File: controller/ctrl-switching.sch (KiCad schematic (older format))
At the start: 35 parts, among them U10 ULN2803A, U11 ULN2803A, U9 74HC595_WITH_PWR

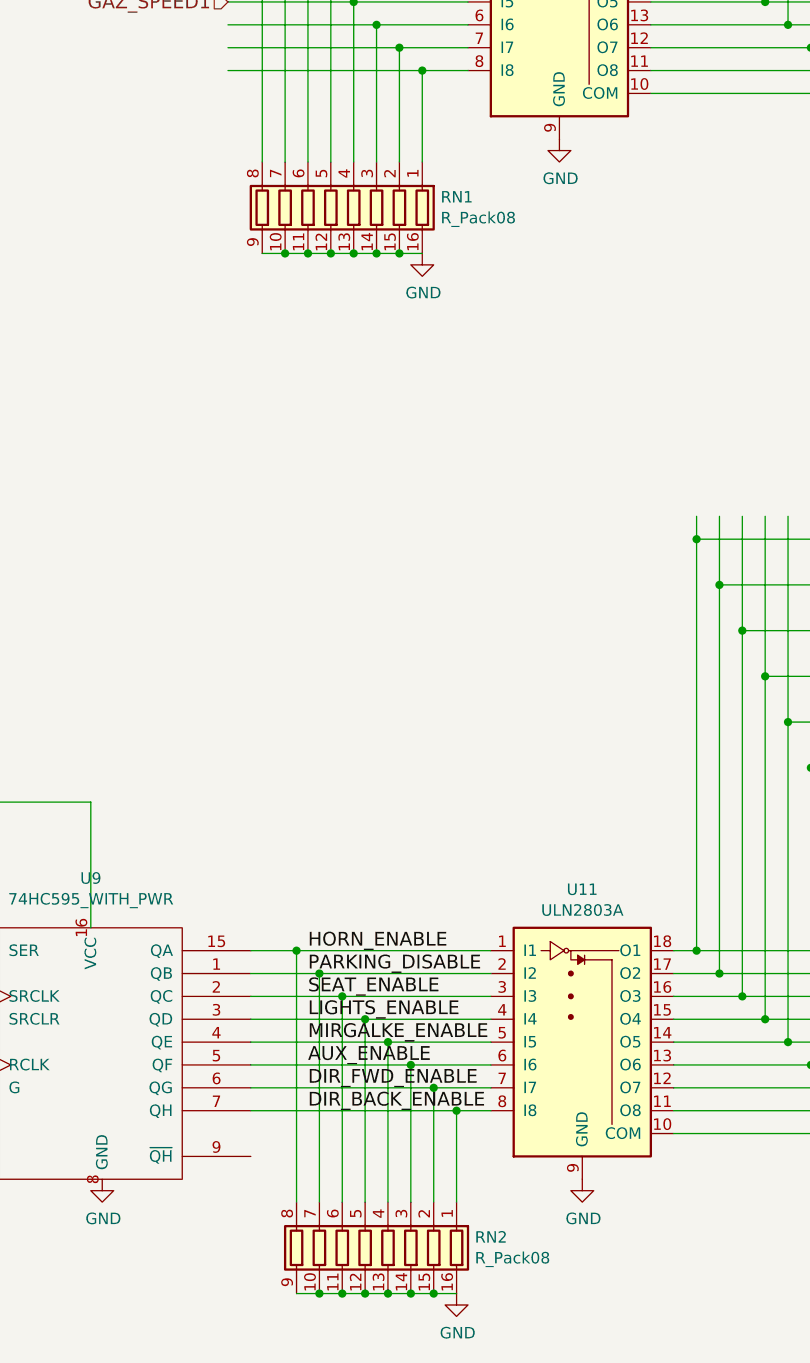
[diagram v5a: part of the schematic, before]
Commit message: Various fixes and comments to the controller board, also making it suitable for non-plated holes.
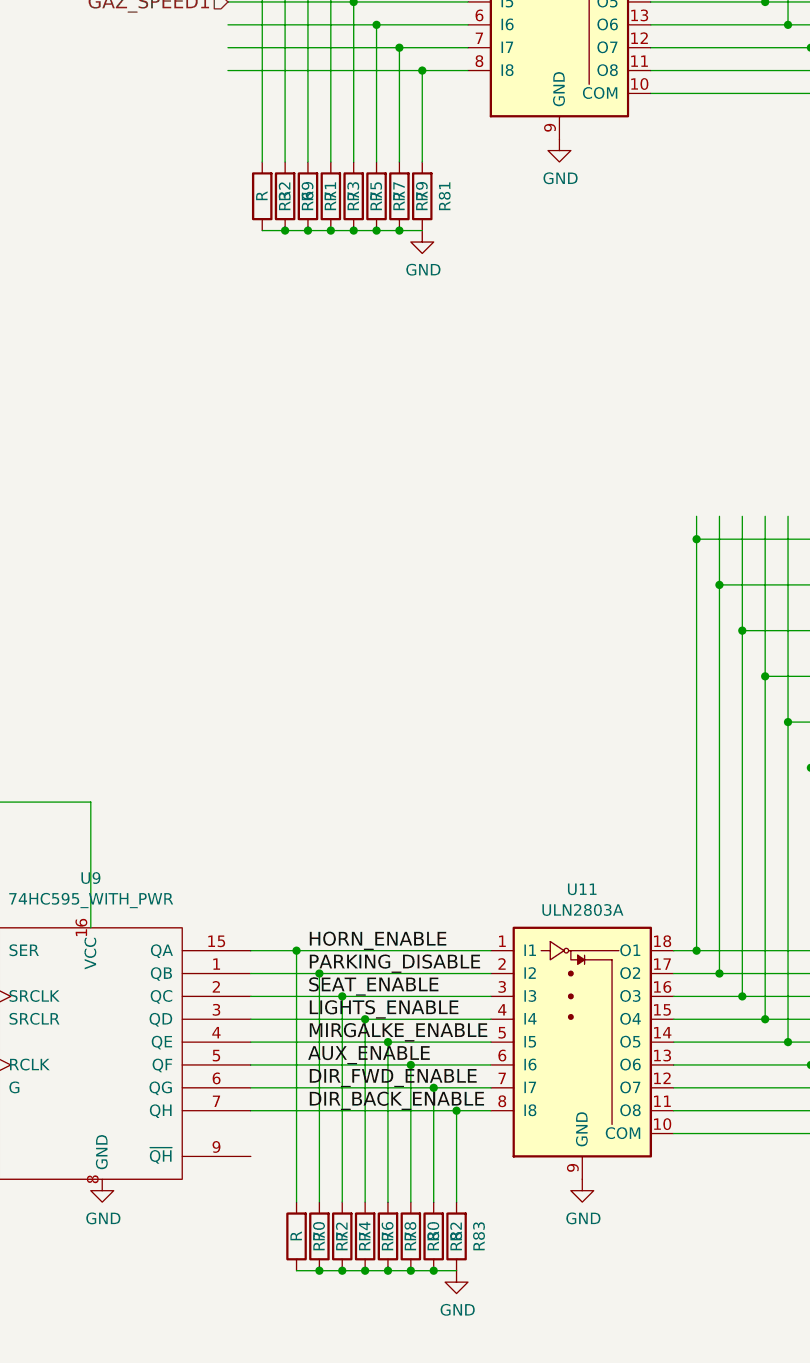
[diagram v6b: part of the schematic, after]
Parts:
- removed RN1, RN2: R_Pack08, Resistors_SMD:R_Array_Convex_8x0602, symbol R_Pack08
- added R32, R69, R70, R71, R72, R73, R74, R75, R76, R77, R78, R79, R80, R81, R82, R83: R, Resistors_SMD:R_0603_HandSoldering, symbol R

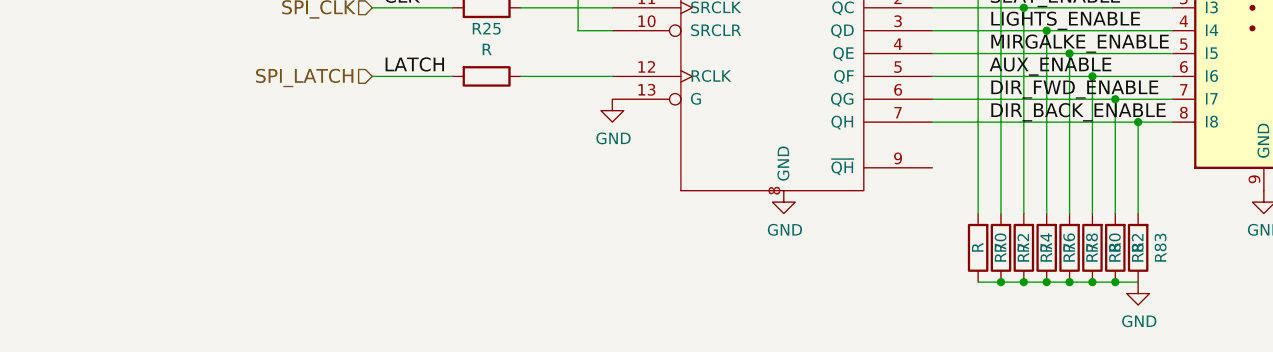
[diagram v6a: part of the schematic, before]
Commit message: add comments with fixes I had to make
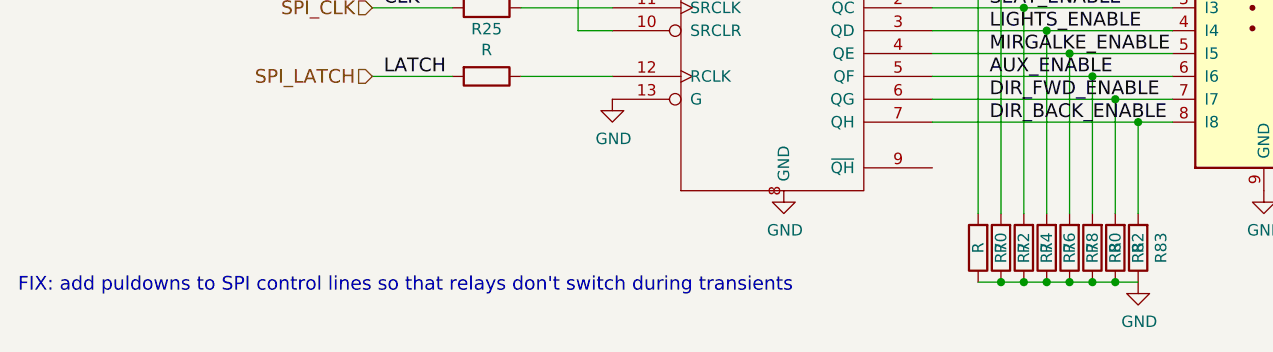
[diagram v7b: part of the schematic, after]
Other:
- note added: "FIX: add puldowns to SPI control lines so that relays don't switch during transients"
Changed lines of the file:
@@
 	-1   0    0    1
 $EndComp
+Text Notes 2500 9800 0    60   ~ 0
+FIX: add puldowns to SPI control lines so that relays don't switch during transients
 $EndSCHEMATC
